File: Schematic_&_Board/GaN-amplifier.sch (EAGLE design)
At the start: 80 parts, among them IC1 LT3080, J1 JOHNSON_SMA_EDGE_LAUNCH_142-0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, J2 JOHNSON_SMA_EDGE_LAUNCH_142-0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, Q1 MMBT3906LT1SMD, T1 IRL3714S, T2 IRL3714S, T3 IRL3714S, T4 IRL3714S, T5 BSP89, U1 TPS7A30XX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

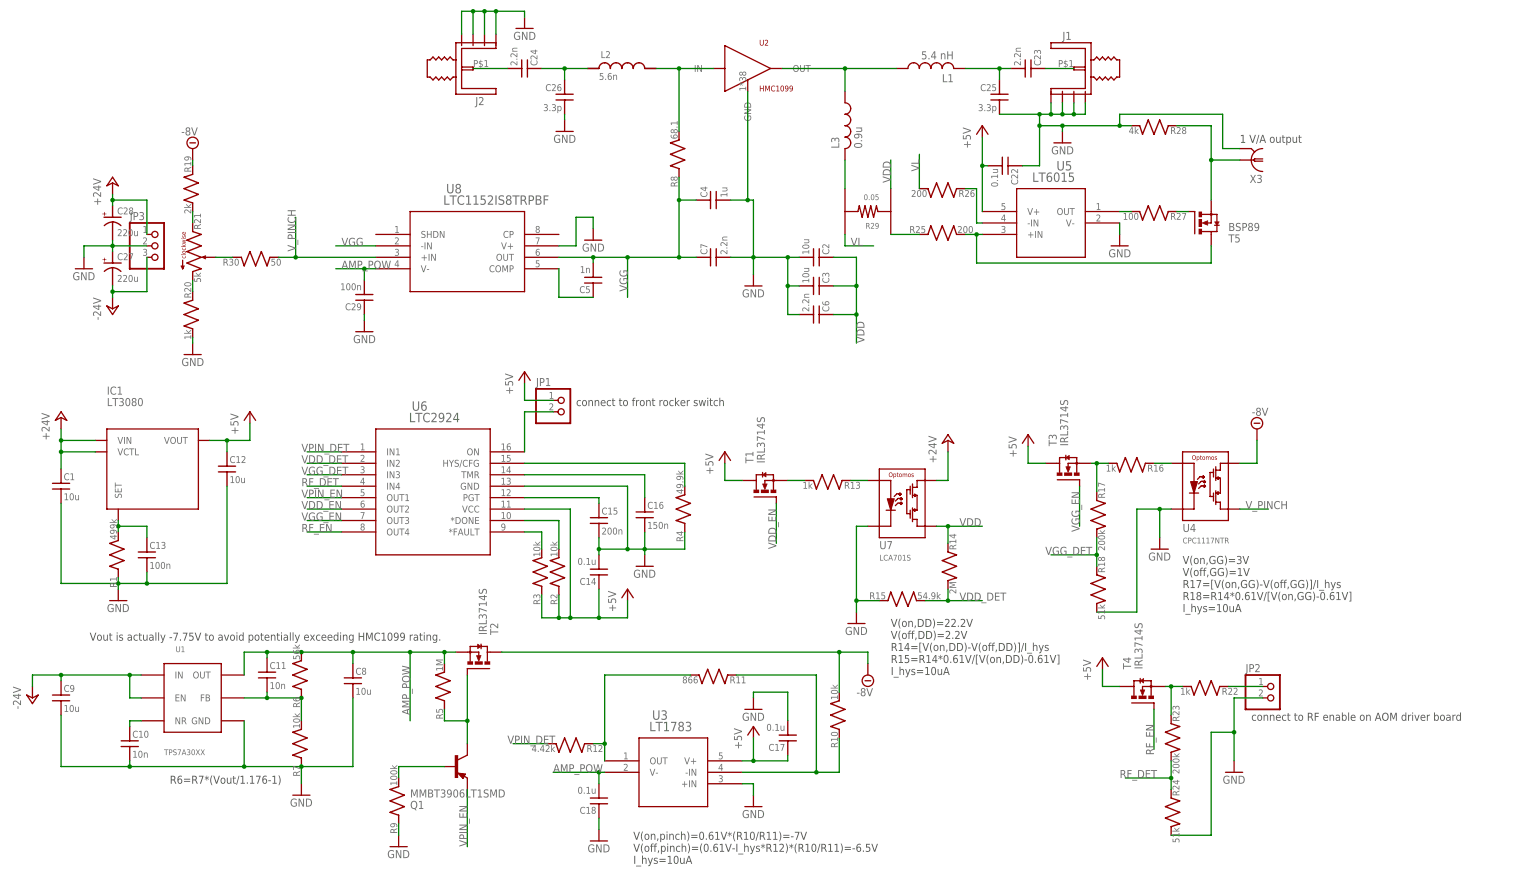
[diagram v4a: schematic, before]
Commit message: Finished Layout, Starting BOM
I've finished the layout up to getting final RF trace widths set (per
manufacturer specs) and started compiling a BOM.

DSB
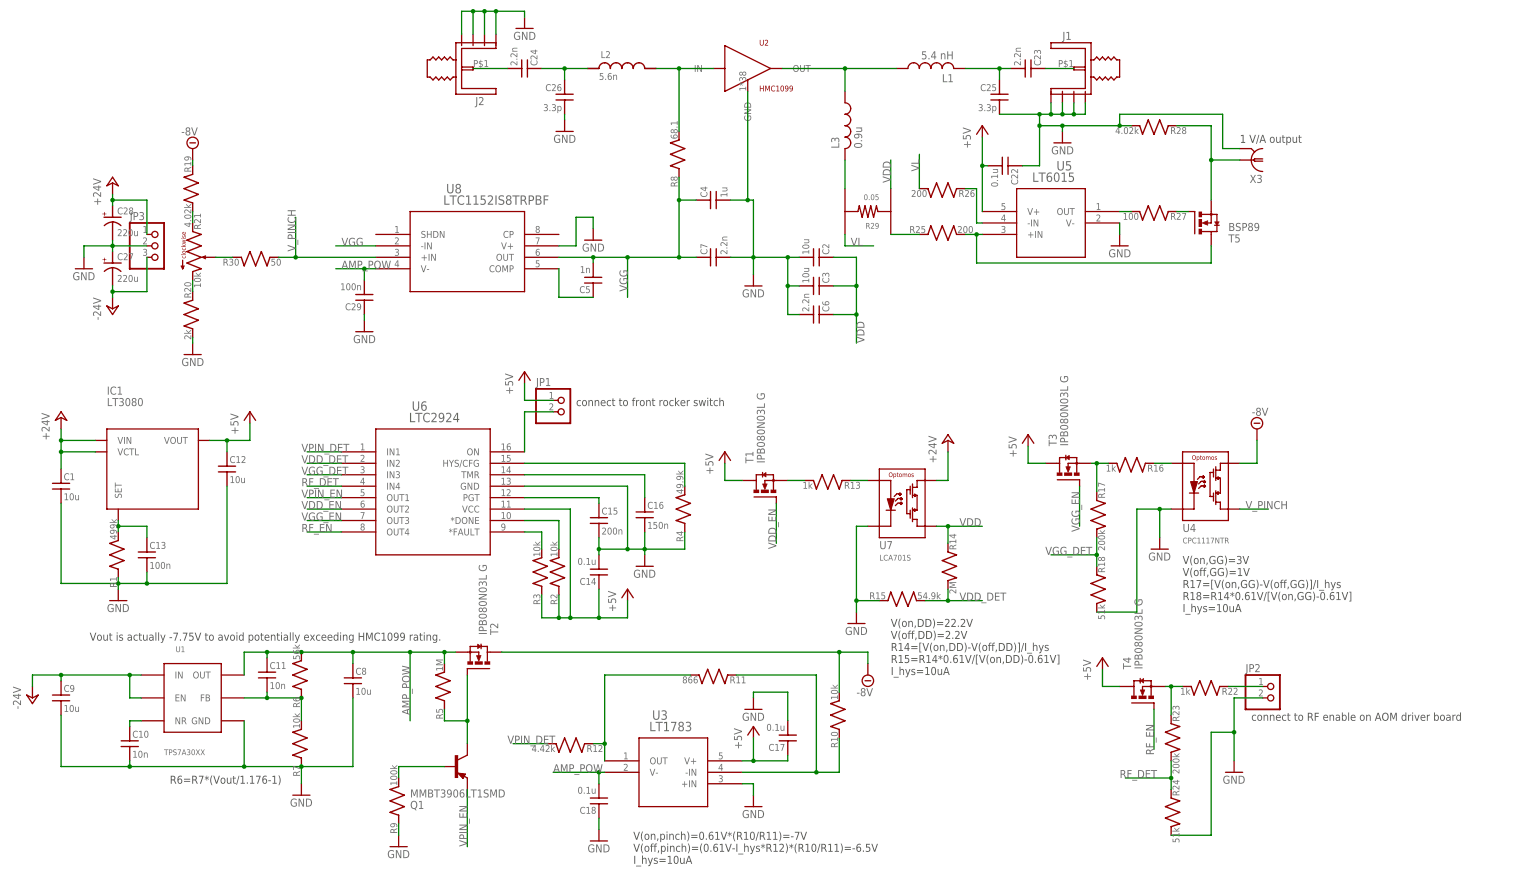
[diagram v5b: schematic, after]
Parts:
- C1, C12: PARTNO (none) -> 445-14417-1-ND
- C13, C14, C17, C18, C22, C29: PARTNO (none) -> 1276-1936-1-ND
- C2, C3: PARTNO (none) -> 587-1818-1-ND
- C23, C24, C6, C7: PARTNO (none) -> 1276-1110-1-ND
- C25, C26: PARTNO (none) -> 581-600S3R3CT
- C27, C28: PARTNO (none) -> PCE3955CT-ND
- IC1: PARTNO (none) -> LT3080EQ#PBF-ND
- JP1, JP2: PARTNO (none) -> A1921-ND
- JP3: PARTNO (none) -> A19470-ND
- L1: PARTNO (none) -> 0906-5JLB
- L2: PARTNO (none) -> 0402CS-5N6XJLU
- L3: PARTNO (none) -> 1008AF-901XKLC
- R1: PARTNO (none) -> P499KHCT-ND
- R10, R2, R3: PARTNO (none) -> P10.0KHCT-ND
- R11: PARTNO (none) -> P866HCT-ND
- R12: PARTNO (none) -> P4.42KHCT-ND
- R13, R16, R22: PARTNO (none) -> P1.00KHCT-ND
- R14: PARTNO (none) -> P2.00MHCT-ND
- R15: PARTNO (none) -> P54.9KHCT-ND
- R17, R23: PARTNO (none) -> P200KHCT-ND
- R18, R24: PARTNO (none) -> P51.0KHCT-ND
- R19: value 2k -> 4.02k; PARTNO (none) -> TNP4.02KAACT-ND
- R20: value 1k -> 2k; PARTNO (none) -> 541-1726-1-ND
- R21: value 5k -> 10k; PARTNO (none) -> 804-1093-ND
- R25, R26: PARTNO (none) -> 541-3049-1-ND
- R27: PARTNO (none) -> P100HCT-ND
- R28: value 4k -> 4.02k; PARTNO (none) -> TNP4.02KAACT-ND
- R29: PARTNO (none) -> LVK12R050DERCT-ND
- R30: PARTNO (none) -> P49.9HCT-ND
- R4: PARTNO (none) -> P49.9KHCT-ND
- R5: PARTNO (none) -> P1.00MHCT-ND
- R6: PARTNO (none) -> P56.0KLCT-ND
- R7: PARTNO (none) -> P10.0KLCT-ND
- R8: PARTNO (none) -> P68.1HCT-ND
- R9: PARTNO (none) -> P100KHCT-ND
- T1, T2, T3, T4: value IRL3714S -> IPB080N03L G; PARTNO (none) -> IPB080N03L GDKR-ND
- T5: PARTNO (none) -> BSP89H6327XTSA1CT-ND
- U1: PARTNO (none) -> 296-27750-1-ND
- U2: PARTNO (none) -> HMC1099LP5DE
- U3: PARTNO (none) -> LT1783HS5#TRMPBFCT-ND
- U4: PARTNO (none) -> CLA268CT-ND
- U5: PARTNO (none) -> LT6015HS5#TRMPBFCT-ND
- U6: PARTNO (none) -> LTC2924IGN#PBF-ND
- U7: PARTNO (none) -> 849-LCA701S
- U8: PARTNO (none) -> LTC1152IS8#PBF-ND
- X3: PARTNO (none) -> A32262-ND

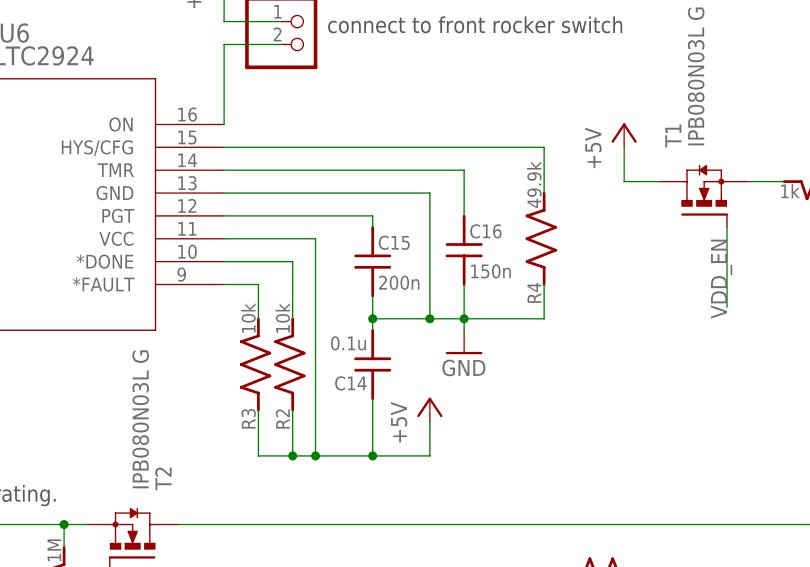
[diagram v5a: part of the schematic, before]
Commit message: Finished BOM
All parts are now added to BOM.

DSB
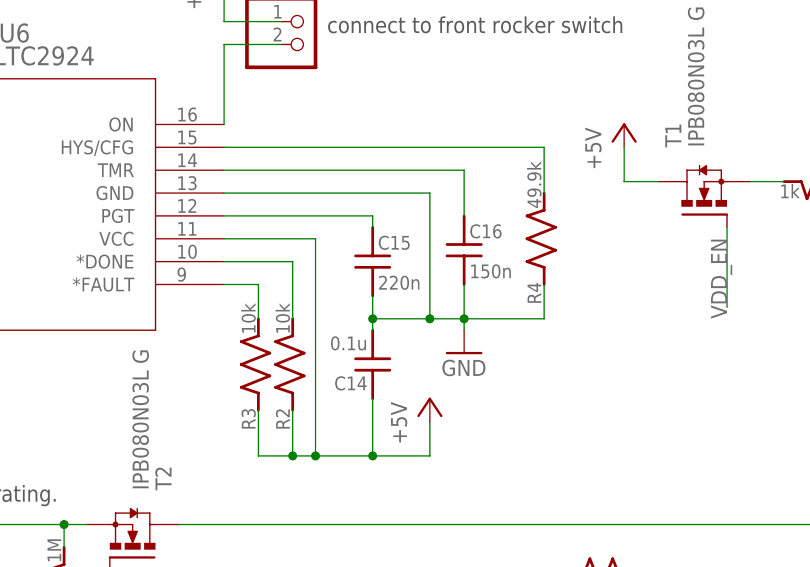
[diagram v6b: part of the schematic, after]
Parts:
- C10, C11: PARTNO (none) -> 1276-1028-1-ND
- C15: value 200n -> 220n; PARTNO (none) -> 1276-2014-1-ND
- C16: PARTNO (none) -> 1276-1973-1-ND
- C4: PARTNO (none) -> 1276-1184-1-ND
- C5: PARTNO (none) -> 1276-1195-1-ND
- C8, C9: PARTNO (none) -> 1276-6767-1-ND
- J1, J2: PARTNO (none) -> J658-ND
- Q1: PARTNO (none) -> MMBT3906LT1GOSCT-ND
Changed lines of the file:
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@@
 <part name="GND4" library="supply1" deviceset="GND" device=""/>
 <part name="SUPPLY1" library="supply2" deviceset="-8V" device=""/>
-<part name="C8" library="jqi_passives" deviceset="C_MLCC_SMD" device="CMLCC_1206" value="10u"/>
-<part name="C9" library="jqi_passives" deviceset="C_MLCC_SMD" device="CMLCC_1206" value="10u"/>
-<part name="C10" library="jqi_passives" deviceset="C_MLCC_SMD" device="CMLCC_0402" value="10n"/>
-<part name="C11" library="jqi_passives" deviceset="C_MLCC_SMD" device="CMLCC_0402" value="10n"/>
+<part name="C8" library="jqi_passives" deviceset="C_MLCC_SMD" device="CMLCC_1206" value="10u">
+<attribute name="PARTNO" value="1276-6767-1-ND"/>
+</part>
+<part name="C9" library="jqi_passives" deviceset="C_MLCC_SMD" device="CMLCC_1206" value="10u">
+<attribute name="PARTNO" value="1276-6767-1-ND"/>
+</part>
+<part name="C10" library="jqi_passives" deviceset="C_MLCC_SMD" device="CMLCC_0402" value="10n">
+<attribute name="PARTNO" value="1276-1028-1-ND"/>
+</part>
+<part name="C11" library="jqi_passives" deviceset="C_MLCC_SMD" device="CMLCC_0402" value="10n">
+<attribute name="PARTNO" value="1276-1028-1-ND"/>
+</part>
 <part name="R6" library="jqi_passives" deviceset="R_SMD" device="R0402" value="56k">
 <attribute name="PARTNO" value="P56.0KLCT-ND"/>
@@
 </part>
 <part name="P+4" library="supply1" deviceset="+5V" device=""/>
-<part name="C15" library="jqi_passives" deviceset="C_MLCC_SMD" device="CMLCC_0603" value="200n"/>
-<part name="C16" library="jqi_passives" deviceset="C_MLCC_SMD" device="CMLCC_0603" value="150n"/>
+<part name="C15" library="jqi_passives" deviceset="C_MLCC_SMD" device="CMLCC_0603" value="220n">
+<attribute name="PARTNO" value="1276-2014-1-ND"/>
+</part>
+<part name="C16" library="jqi_passives" deviceset="C_MLCC_SMD" device="CMLCC_0603" value="150n">
+<attribute name="PARTNO" value="1276-1973-1-ND"/>
+</part>
 <part name="R4" library="jqi_passives" deviceset="R_SMD" device="R0603" value="49.9k">
 <attribute name="PARTNO" value="P49.9KHCT-ND"/>
@@
 <attribute name="PARTNO" value="CLA268CT-ND"/>
 </part>
-<part name="Q1" library="transistor-pnp" deviceset="MMBT3906*" device="SMD" technology="LT1"/>
+<part name="Q1" library="transistor-pnp" deviceset="MMBT3906*" device="SMD" technology="LT1">
+<attribute name="PARTNO" value="MMBT3906LT1GOSCT-ND"/>
+</part>
 <part name="R5" library="jqi_passives" deviceset="R_SMD" device="R0603" value="1M">
 <attribute name="PARTNO" value="P1.00MHCT-ND"/>
@@
 <attribute name="PARTNO" value="804-1093-ND"/>
 </part>
-<part name="J1" library="connector-jqi" deviceset="JOHNSON_SMA_EDGE_LAUNCH_142-0701-851" device=""/>
-<part name="J2" library="connector-jqi" deviceset="JOHNSON_SMA_EDGE_LAUNCH_142-0701-851" device=""/>
+<part name="J1" library="connector-jqi" deviceset="JOHNSON_SMA_EDGE_LAUNCH_142-0701-851" device="">
+<attribute name="PARTNO" value="J658-ND"/>
+</part>
+<part name="J2" library="connector-jqi" deviceset="JOHNSON_SMA_EDGE_LAUNCH_142-0701-851" device="">
+<attribute name="PARTNO" value="J658-ND"/>
+</part>
 <part name="GND17" library="supply1" deviceset="GND" device=""/>
 <part name="U8" library="linear-technology-jqi" deviceset="LTC1152IS8TRPBF" device="">
 <attribute name="PARTNO" value="LTC1152IS8#PBF-ND"/>
 </part>
-<part name="C4" library="jqi_passives" deviceset="C_MLCC_SMD" device="CMLCC_0603" value="1u"/>
-<part name="C5" library="jqi_passives" deviceset="C_MLCC_SMD" device="CMLCC_0603" value="1n"/>
+<part name="C4" library="jqi_passives" deviceset="C_MLCC_SMD" device="CMLCC_0603" value="1u">
+<attribute name="PARTNO" value="1276-1184-1-ND"/>
+</part>
+<part name="C5" library="jqi_passives" deviceset="C_MLCC_SMD" device="CMLCC_0603" value="1n">
+<attribute name="PARTNO" value="1276-1195-1-ND"/>
+</part>
 <part name="R30" library="jqi_passives" deviceset="R_SMD" device="R0603" value="50">
 <attribute name="PARTNO" value="P49.9HCT-ND"/>
@@
 <instance part="GND4" gate="1" x="100.33" y="172.72"/>
 <instance part="SUPPLY1" gate="G$1" x="125.73" y="86.36"/>
-<instance part="C8" gate="G$1" x="11.43" y="86.36"/>
-<instance part="C9" gate="G$1" x="-53.34" y="82.55"/>
-<instance part="C10" gate="G$1" x="-38.1" y="72.39"/>
-<instance part="C11" gate="G$1" x="-7.62" y="87.63"/>
+<instance part="C8" gate="G$1" x="11.43" y="86.36">
+<attribute name="PARTNO" x="11.43" y="86.36" size="1.778" layer="96" display="off"/>
+</instance>
+<instance part="C9" gate="G$1" x="-53.34" y="82.55">
+<attribute name="PARTNO" x="-53.34" y="82.55" size="1.778" layer="96" display="off"/>
+</instance>
+<instance part="C10" gate="G$1" x="-38.1" y="72.39">
+<attribute name="PARTNO" x="-38.1" y="72.39" size="1.778" layer="96" display="off"/>
+</instance>
+<instance part="C11" gate="G$1" x="-7.62" y="87.63">
+<attribute name="PARTNO" x="-7.62" y="87.63" size="1.778" layer="96" display="off"/>
+</instance>
 <instance part="R6" gate="G$1" x="0" y="86.36" rot="R90">
 <attribute name="PARTNO" x="0" y="86.36" size="1.778" layer="96" display="off"/>
@@
 </instance>
 <instance part="P+4" gate="1" x="49.53" y="153.67"/>
-<instance part="C15" gate="G$1" x="66.04" y="121.92"/>
-<instance part="C16" gate="G$1" x="76.2" y="123.19"/>
+<instance part="C15" gate="G$1" x="66.04" y="121.92">
+<attribute name="PARTNO" x="66.04" y="121.92" size="1.778" layer="96" display="off"/>
+</instance>
+<instance part="C16" gate="G$1" x="76.2" y="123.19">
+<attribute name="PARTNO" x="76.2" y="123.19" size="1.778" layer="96" display="off"/>
+</instance>
 <instance part="R4" gate="G$1" x="85.09" y="123.19" rot="R90">
 <attribute name="PARTNO" x="85.09" y="123.19" size="1.778" layer="96" display="off"/>
@@
 <attribute name="PARTNO" x="200.66" y="128.27" size="1.778" layer="96" display="off"/>
 </instance>
-<instance part="Q1" gate="G$1" x="34.29" y="66.04" rot="MR180"/>
+<instance part="Q1" gate="G$1" x="34.29" y="66.04" rot="MR180">
+<attribute name="PARTNO" x="34.29" y="66.04" size="1.778" layer="96" display="off"/>
+</instance>
 <instance part="R5" gate="G$1" x="31.75" y="83.82" rot="R90">
 <attribute name="PARTNO" x="31.75" y="83.82" size="1.778" layer="96" display="off"/>
@@
 <attribute name="PARTNO" x="-24.13" y="181.61" size="1.778" layer="96" display="off"/>
 </instance>
-<instance part="J1" gate="G$1" x="173.99" y="220.98"/>
-<instance part="J2" gate="G$1" x="35.56" y="220.98" rot="R180"/>
+<instance part="J1" gate="G$1" x="173.99" y="220.98">
+<attribute name="PARTNO" x="173.99" y="220.98" size="1.778" layer="96" display="off"/>
+</instance>
+<instance part="J2" gate="G$1" x="35.56" y="220.98" rot="R180">
+<attribute name="PARTNO" x="35.56" y="220.98" size="1.778" layer="96" display="off"/>
+</instance>
 <instance part="GND17" gate="1" x="49.53" y="229.87" rot="MR0"/>
 <instance part="U8" gate="A" x="16.51" y="184.15">
 <attribute name="PARTNO" x="16.51" y="184.15" size="1.778" layer="96" display="off"/>
 </instance>
-<instance part="C4" gate="G$1" x="90.17" y="191.77" rot="R90"/>
-<instance part="C5" gate="G$1" x="64.77" y="172.72" rot="R180"/>
+<instance part="C4" gate="G$1" x="90.17" y="191.77" rot="R90">
+<attribute name="PARTNO" x="90.17" y="191.77" size="1.778" layer="96" display="off"/>
+</instance>
+<instance part="C5" gate="G$1" x="64.77" y="172.72" rot="R180">
+<attribute name="PARTNO" x="64.77" y="172.72" size="1.778" layer="96" display="off"/>
+</instance>
 <instance part="R30" gate="G$1" x="-10.16" y="179.07" rot="MR180">
 <attribute name="PARTNO" x="-10.16" y="179.07" size="1.778" layer="96" display="off"/>

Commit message: Finalizing Design
I've almost finalized the design. Just need to order the HMC1099 and
ensure that Macrofab can do the job properly.

DSB
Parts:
- U2: PARTNO HMC1099LP5DE -> 584-HMC1099LP5DE
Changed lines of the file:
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@@
 </part>
 <part name="U2" library="rf-jqi" deviceset="HMC1099" device="" value="HMC1099">
-<attribute name="PARTNO" value="HMC1099LP5DE"/>
+<attribute name="PARTNO" value="584-HMC1099LP5DE"/>
 </part>
 <part name="T1" library="transistor-jqi" deviceset="IRL3714" device="" value="IPB080N03L G">

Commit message: Updated BOM and Mirrored Parts
Changed BOM for better compatibility with MacroFab. Changed the
through-hole components to populate on the bottom of the board.

DSB
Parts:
- C1, C12: PARTNO 445-14417-1-ND -> C2012X5R1V106K085AC
- C10, C11: PARTNO 1276-1028-1-ND -> CL05B103KB5NNNC
- C13, C14, C17, C18, C22, C29: PARTNO 1276-1936-1-ND -> CL10B104KB8SFNC
- C15: PARTNO 1276-2014-1-ND -> CL10B224KP8NNNC
- C16: PARTNO 1276-1973-1-ND -> CL10B154KP8NNNC
- C2, C3: PARTNO 587-1818-1-ND -> UMK325C7106MM-T
- C23, C24, C6, C7: PARTNO 1276-1110-1-ND -> CL10B222KB8NNNC
- C25, C26: PARTNO 581-600S3R3CT -> 600S3R3CT250XT
- C27, C28: PARTNO PCE3955CT-ND -> EEE-1VA221UP
- C4: PARTNO 1276-1184-1-ND -> CL10B105KA8NNNC
- C5: PARTNO 1276-1195-1-ND -> CL10B102KA8NNNC
- C8, C9: PARTNO 1276-6767-1-ND -> GMK316AB7106KL-TR
- IC1: PARTNO LT3080EQ#PBF-ND -> LT3080EQ#PBF
- J1, J2: PARTNO J658-ND -> 142-0701-851
- JP1, JP2: PARTNO A1921-ND -> 640456-2
- JP3: PARTNO A19470-ND -> 640456-3
- Q1: PARTNO MMBT3906LT1GOSCT-ND -> MMBT3906LT1G
- R1: PARTNO P499KHCT-ND -> ERJ-3EKF4993V
- R10, R2, R3: PARTNO P10.0KHCT-ND -> ERJ-3EKF1002V
- R11: PARTNO P866HCT-ND -> ERJ-3EKF8660V
- R12: PARTNO P4.42KHCT-ND -> ERJ-3EKF4421V
- R13, R16, R22: PARTNO P1.00KHCT-ND -> ERJ-3EKF1001V
- R14: PARTNO P2.00MHCT-ND -> ERJ-3EKF2004V
- R15: PARTNO P54.9KHCT-ND -> ERJ-3EKF5492V
- R17, R23: PARTNO P200KHCT-ND -> ERJ-3EKF2003V
- R18, R24: PARTNO P51.0KHCT-ND -> ERJ-3EKF5102V
- R19, R28: PARTNO TNP4.02KAACT-ND -> TNPW06034K02BEEA
- R20: PARTNO 541-1726-1-ND -> TNPW06032K00BXEN
- R21: PARTNO 804-1093-ND -> Y006910K0000J9L
- R25, R26: PARTNO 541-3049-1-ND -> TNPW0603200RBEEA
- R27: PARTNO P100HCT-ND -> ERJ-3EKF1000V
- R29: PARTNO LVK12R050DERCT-ND -> LVK12R050DER
- R30: PARTNO P49.9HCT-ND -> ERJ-3EKF49R9V
- R4: PARTNO P49.9KHCT-ND -> ERJ-3EKF4992V
- R5: PARTNO P1.00MHCT-ND -> ERJ-3EKF1004V
- R6: PARTNO P56.0KLCT-ND -> ERJ-2RKF5602X
- R7: PARTNO P10.0KLCT-ND -> ERJ-2RKF1002X
- R8: PARTNO P68.1HCT-ND -> ERJ-3EKF68R1V
- R9: PARTNO P100KHCT-ND -> ERJ-3EKF1003V
- T1, T2, T3, T4: PARTNO IPB080N03L GDKR-ND -> IPB080N03L G
- T5: PARTNO BSP89H6327XTSA1CT-ND -> BSP89H6327XTSA1
- U1: PARTNO 296-27750-1-ND -> TPS7A3001DGNR
- U2: PARTNO 584-HMC1099LP5DE -> HMC1099LP5DE
- U3: PARTNO LT1783HS5#TRMPBFCT-ND -> LT1783HS5#TRMPBF
- U4: PARTNO CLA268CT-ND -> CPC1117NTR
- U5: PARTNO LT6015HS5#TRMPBFCT-ND -> LT6015HS5#TRMPBF
- U6: PARTNO LTC2924IGN#PBF-ND -> LTC2924IGN#PBF
- U7: PARTNO 849-LCA701S -> LCA701S
- U8: PARTNO LTC1152IS8#PBF-ND -> LTC1152IS8#PBF
- X3: PARTNO A32262-ND -> 5227222-3
